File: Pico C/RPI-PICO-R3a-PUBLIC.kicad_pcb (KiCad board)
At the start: 2 copper layers, 53.7 x 21 mm, 54 parts, among them IC1 W25Q16JVUXIQ, J3 USB_C_Receptacle_USB2.0_16P, J4 SM03B-SRSS-TB, Q1 DMG1012T-7, U1 RP2040, U2 RT6150B-33GQW, Y1 ECS-120-8-33-JGN-TR

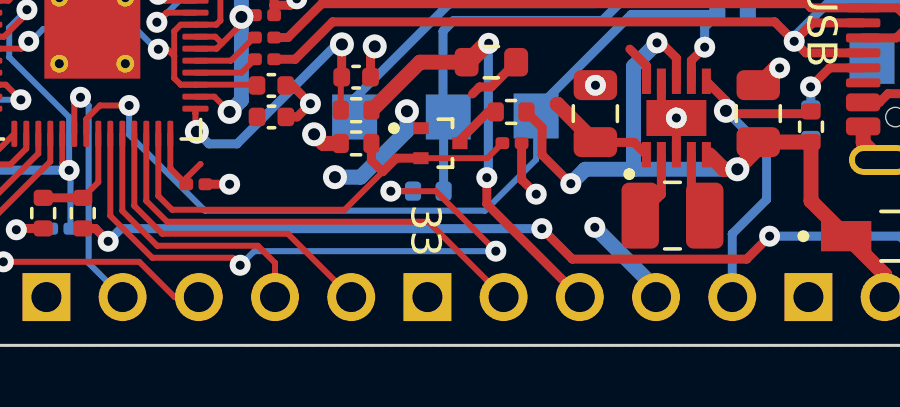
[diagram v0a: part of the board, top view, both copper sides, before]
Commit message: Add files via upload
Corrected pin 33 to actually be GND instead of a NC to GNDA.
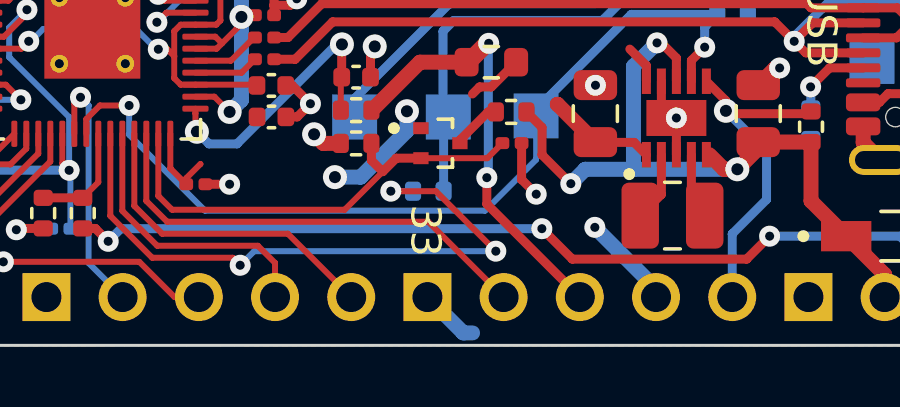
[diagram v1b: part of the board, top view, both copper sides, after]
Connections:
- J2 pad 33: GNDA -> GND
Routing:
- net GND: track 40.8 -> 42.8 mm

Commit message: Add files via upload
Updated component references to more closely match the original Pico.
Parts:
- renumbered R15 to R14, R14 to R15, IC1 to U3, Y1 to X1
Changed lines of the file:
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@@
 	(net 12 "/3V3_EN")
 	(net 13 "Net-(J3-CC1)")
-	(net 14 "unconnected-(IC1-EP-Pad9)")
+	(net 14 "unconnected-(U3-EP-Pad9)")
 	(net 15 "Net-(Q1-D)")
 	(net 16 "+1V1")
@@
 		(descr "Resistor SMD 0201 (0603 Metric), square (rectangular) end terminal, IPC_7351 nominal, (Body size source: https://www.vishay.com/docs/20052/crcw0201e3.pdf), generated with kicad-footprint-generator")
 		(tags "resistor")
-		(property "Reference" "R15"
+		(property "Reference" "R14"
 			(at 0 -1.05 0)
 			(layer "F.Fab")
@@
 		(descr "Resistor SMD 0201 (0603 Metric), square (rectangular) end terminal, IPC_7351 nominal, (Body size source: https://www.vishay.com/docs/20052/crcw0201e3.pdf), generated with kicad-footprint-generator")
 		(tags "resistor")
-		(property "Reference" "R14"
+		(property "Reference" "R15"
 			(at 0 -1.05 0)
 			(layer "F.Fab")
@@
 		(layer "F.Cu")
 		(at 135.625 97.525 -90)
-		(property "Reference" "Y1"
+		(property "Reference" "X1"
 			(at 0.03 -2.1 90)
 			(layer "F.Fab")
@@
 		(at 156.6 97)
 		(descr "<b>USON 2x3x0.6-mm</b><br>")
-		(property "Reference" "IC1"
+		(property "Reference" "U3"
 			(at 0 0 0)
 			(layer "F.Fab")
@@
 			(size 1.65 0.25)
 			(layers "F.Cu" "F.Paste" "F.Mask")
-			(net 14 "unconnected-(IC1-EP-Pad9)")
+			(net 14 "unconnected-(U3-EP-Pad9)")
 			(pinfunction "EP")
 			(pintype "bidirectional+no_connect")

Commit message: Add files via upload
Changed resistor reference numbers to match the real Pico H.
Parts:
- renumbered R3 to R1, R12 to R10, R13 to R11, R14 to R12, R15 to R13, R16 to R14, R17 to R15, R1 to R16, R2 to R17, R4 to R2, R5 to R3, R6 to R4, R7 to R5, R8 to R6, R9 to R7, R10 to R8, R11 to R9
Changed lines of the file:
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@@
 	(net 62 "XOUT")
 	(net 63 "/RP2040/USB_DMX")
-	(net 64 "Net-(R13-Pad2)")
+	(net 64 "Net-(R11-Pad2)")
 	(footprint "Resistor_SMD:R_0402_1005Metric"
 		(layer "F.Cu")
@@
 		(descr "Resistor SMD 0402 (1005 Metric), square (rectangular) end terminal, IPC_7351 nominal, (Body size source: IPC-SM-782 page 72, https://www.pcb-3d.com/wordpress/wp-content/uploads/ipc-sm-782a_amendment_1_and_2.pdf), generated with kicad-footprint-generator")
 		(tags "resistor")
-		(property "Reference" "R6"
+		(property "Reference" "R4"
 			(at 0 -1.17 0)
 			(layer "F.Fab")
@@
 		(descr "Resistor SMD 0402 (1005 Metric), square (rectangular) end terminal, IPC_7351 nominal, (Body size source: IPC-SM-782 page 72, https://www.pcb-3d.com/wordpress/wp-content/uploads/ipc-sm-782a_amendment_1_and_2.pdf), generated with kicad-footprint-generator")
 		(tags "resistor")
-		(property "Reference" "R7"
+		(property "Reference" "R5"
 			(at 0 -1.17 0)
 			(layer "F.Fab")
@@
 		(descr "Resistor SMD 0402 (1005 Metric), square (rectangular) end terminal, IPC_7351 nominal, (Body size source: IPC-SM-782 page 72, https://www.pcb-3d.com/wordpress/wp-content/uploads/ipc-sm-782a_amendment_1_and_2.pdf), generated with kicad-footprint-generator")
 		(tags "resistor")
-		(property "Reference" "R12"
+		(property "Reference" "R10"
 			(at 0 -1.17 90)
 			(layer "F.Fab")
@@
 		(descr "Resistor SMD 0201 (0603 Metric), square (rectangular) end terminal, IPC_7351 nominal, (Body size source: https://www.vishay.com/docs/20052/crcw0201e3.pdf), generated with kicad-footprint-generator")
 		(tags "resistor")
-		(property "Reference" "R14"
+		(property "Reference" "R12"
 			(at 0 -1.05 0)
 			(layer "F.Fab")
@@
 		(descr "Resistor SMD 0402 (1005 Metric), square (rectangular) end terminal, IPC_7351 nominal, (Body size source: IPC-SM-782 page 72, https://www.pcb-3d.com/wordpress/wp-content/uploads/ipc-sm-782a_amendment_1_and_2.pdf), generated with kicad-footprint-generator")
 		(tags "resistor")
-		(property "Reference" "R3"
+		(property "Reference" "R1"
 			(at 0 -1.17 90)
 			(layer "F.Fab")
@@
 		(descr "Resistor SMD 0603 (1608 Metric), square (rectangular) end terminal, IPC_7351 nominal, (Body size source: IPC-SM-782 page 72, https://www.pcb-3d.com/wordpress/wp-content/uploads/ipc-sm-782a_amendment_1_and_2.pdf), generated with kicad-footprint-generator")
 		(tags "resistor")
-		(property "Reference" "R9"
+		(property "Reference" "R7"
 			(at 0 -1.43 0)
 			(layer "F.Fab")
@@
 		(descr "Resistor SMD 0402 (1005 Metric), square (rectangular) end terminal, IPC_7351 nominal, (Body size source: IPC-SM-782 page 72, https://www.pcb-3d.com/wordpress/wp-content/uploads/ipc-sm-782a_amendment_1_and_2.pdf), generated with kicad-footprint-generator")
 		(tags "resistor")
-		(property "Reference" "R17"
+		(property "Reference" "R15"
 			(at 0 -1.17 90)
 			(layer "F.Fab")
@@
 		(descr "Resistor SMD 0402 (1005 Metric), square (rectangular) end terminal, IPC_7351 nominal, (Body size source: IPC-SM-782 page 72, https://www.pcb-3d.com/wordpress/wp-content/uploads/ipc-sm-782a_amendment_1_and_2.pdf), generated with kicad-footprint-generator")
 		(tags "resistor")
-		(property "Reference" "R16"
+		(property "Reference" "R14"
 			(at 0 -1.17 90)
 			(layer "F.Fab")
@@
 		(descr "Resistor SMD 0402 (1005 Metric), square (rectangular) end terminal, IPC_7351 nominal, (Body size source: IPC-SM-782 page 72, https://www.pcb-3d.com/wordpress/wp-content/uploads/ipc-sm-782a_amendment_1_and_2.pdf), generated with kicad-footprint-generator")
 		(tags "resistor")
-		(property "Reference" "R8"
+		(property "Reference" "R6"
 			(at 0 -1.17 0)
 			(layer "F.Fab")
@@
 		(descr "Resistor SMD 0402 (1005 Metric), square (rectangular) end terminal, IPC_7351 nominal, (Body size source: IPC-SM-782 page 72, https://www.pcb-3d.com/wordpress/wp-content/uploads/ipc-sm-782a_amendment_1_and_2.pdf), generated with kicad-footprint-generator")
 		(tags "resistor")
-		(property "Reference" "R4"
+		(property "Reference" "R2"
 			(at 0 -1.27 90)
 			(layer "F.Fab")
@@
 		(descr "Resistor SMD 0201 (0603 Metric), square (rectangular) end terminal, IPC_7351 nominal, (Body size source: https://www.vishay.com/docs/20052/crcw0201e3.pdf), generated with kicad-footprint-generator")
 		(tags "resistor")
-		(property "Reference" "R15"
+		(property "Reference" "R13"
 			(at 0 -1.05 0)
 			(layer "F.Fab")
@@
 			(size 1.05 0.65)
 			(layers "F.Cu" "F.Paste" "F.Mask")
-			(net 64 "Net-(R13-Pad2)")
+			(net 64 "Net-(R11-Pad2)")
 			(pinfunction "1")
 			(pintype "unspecified")
@@
 			(size 1.05 0.65)
 			(layers "F.Cu" "F.Paste" "F.Mask")
-			(net 64 "Net-(R13-Pad2)")
+			(net 64 "Net-(R11-Pad2)")
 			(pinfunction "2")
 			(pintype "unspecified")
@@
 		(descr "Resistor SMD 0402 (1005 Metric), square (rectangular) end terminal, IPC_7351 nominal, (Body size source: IPC-SM-782 page 72, https://www.pcb-3d.com/wordpress/wp-content/uploads/ipc-sm-782a_amendment_1_and_2.pdf), generated with kicad-footprint-generator")
 		(tags "resistor")
-		(property "Reference" "R13"
+		(property "Reference" "R11"
 			(at 0 -1.17 0)
 			(layer "F.Fab")
@@
 			(layers "F.Cu" "F.Paste" "F.Mask")
 			(roundrect_rratio 0.25)
-			(net 64 "Net-(R13-Pad2)")
+			(net 64 "Net-(R11-Pad2)")
 			(pintype "passive")
 		)
@@
 		(descr "Resistor SMD 0402 (1005 Metric), square (rectangular) end terminal, IPC_7351 nominal, (Body size source: IPC-SM-782 page 72, https://www.pcb-3d.com/wordpress/wp-content/uploads/ipc-sm-782a_amendment_1_and_2.pdf), generated with kicad-footprint-generator")
 		(tags "resistor")
-		(property "Reference" "R11"
+		(property "Reference" "R9"
 			(at 0 -1.17 0)
 			(layer "F.Fab")
@@
 		(descr "Resistor SMD 0402 (1005 Metric), square (rectangular) end terminal, IPC_7351 nominal, (Body size source: IPC-SM-782 page 72, https://www.pcb-3d.com/wordpress/wp-content/uploads/ipc-sm-782a_amendment_1_and_2.pdf), generated with kicad-footprint-generator")
 		(tags "resistor")
-		(property "Reference" "R10"
+		(property "Reference" "R8"
 			(at 0.062879 1.301342 0)
 			(layer "B.Fab")
@@
 			(size 1.5 1.5)
 			(layers "B.Cu" "B.Mask")
-			(net 64 "Net-(R13-Pad2)")
+			(net 64 "Net-(R11-Pad2)")
 			(pinfunction "1")
 			(pintype "passive")
@@
 		(descr "Resistor SMD 0402 (1005 Metric), square (rectangular) end terminal, IPC_7351 nominal, (Body size source: IPC-SM-782 page 72, https://www.pcb-3d.com/wordpress/wp-content/uploads/ipc-sm-782a_amendment_1_and_2.pdf), generated with kicad-footprint-generator")
 		(tags "resistor")
-		(property "Reference" "R5"
+		(property "Reference" "R3"
 			(at 0 1.17 0)
 			(layer "B.Fab")
@@
 		(descr "Resistor SMD 0402 (1005 Metric), square (rectangular) end terminal, IPC_7351 nominal, (Body size source: IPC-SM-782 page 72, https://www.pcb-3d.com/wordpress/wp-content/uploads/ipc-sm-782a_amendment_1_and_2.pdf), generated with kicad-footprint-generator")
 		(tags "resistor")
-		(property "Reference" "R2"
+		(property "Reference" "R17"
 			(at 0 -1.25 90)
 			(layer "B.Fab")
@@
 		(descr "Resistor SMD 0402 (1005 Metric), square (rectangular) end terminal, IPC_7351 nominal, (Body size source: IPC-SM-782 page 72, https://www.pcb-3d.com/wordpress/wp-content/uploads/ipc-sm-782a_amendment_1_and_2.pdf), generated with kicad-footprint-generator")
 		(tags "resistor")
-		(property "Reference" "R1"
+		(property "Reference" "R16"
 			(at 0.153641 1.27 90)
 			(layer "B.Fab")

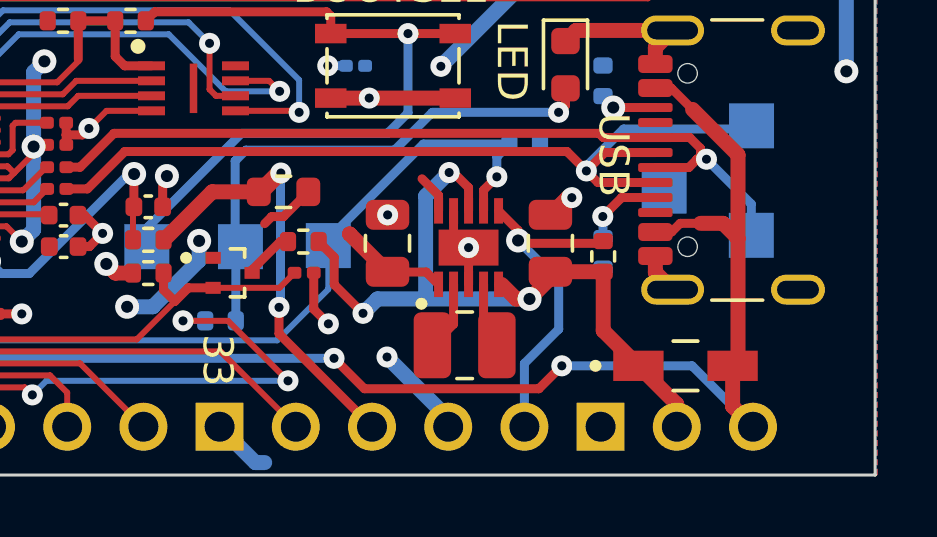
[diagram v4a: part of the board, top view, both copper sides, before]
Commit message: Footprint Modifications
Changed the footprints to use included KiCad models where possible, removed unnecessary STEP files.
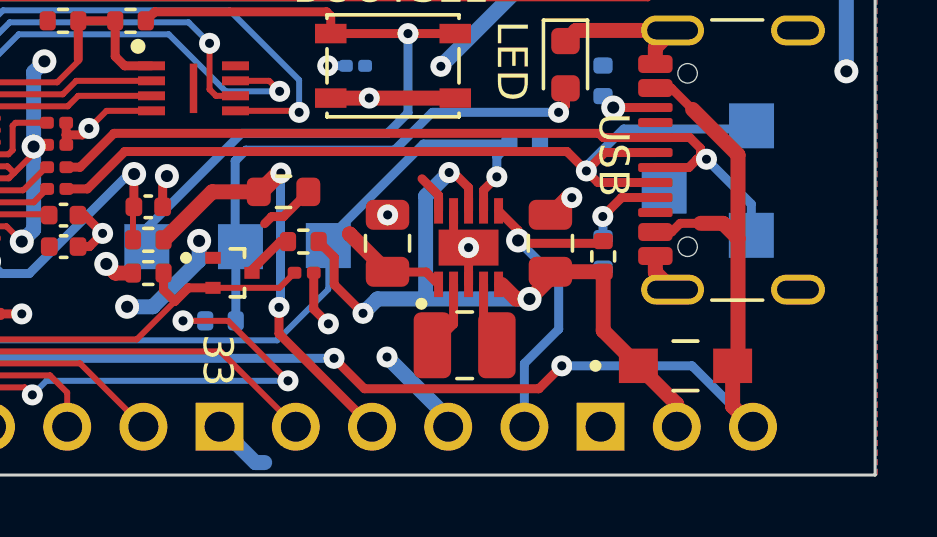
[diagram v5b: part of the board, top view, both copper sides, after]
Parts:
- removed S1: PTS810 SJM 250 SMTR LFS, Pico_C:SW_SPST_PTS810
- added SW1: PTS810 SJM 250 SMTR LFSPTS810 SJM 250 SMTR LFS, Pico_C:SW_SPST_PTS810, F.Cu at (163.2, 96.2)

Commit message: Updated schematic for crystal
Updated the schematic symbol for the 12MHz crystal to be a KiCad included symbol.
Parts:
- removed X1: ECS-120-8-33-JGN-TR, Pico_C:XTAL_ECS-120-8-33-JGN-TR
- added Y1: ECS-120-8-33-JGN-TR, Pico_C:XTAL_ECS-120-8-33-JGN-TR, F.Cu at (135.6, 97.5)
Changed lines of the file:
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@@
 		)
 	)
+	(footprint "Pico_C:XTAL_ECS-120-8-33-JGN-TR"
+		(layer "F.Cu")
+		(at 135.625 97.525 -90)
+		(property "Reference" "Y1"
+			(at 0.03 -2.1 90)
+			(layer "F.Fab")
+			(effects
+				(font
+					(size 0.5 0.5)
+					(thickness 0.1)
+					(bold yes)
+				)
+			)
+		)
+		(property "Value" "ECS-120-8-33-JGN-TR"
+			(at -0.01 2.2 90)
+			(layer "F.Fab")
+			(effects
+				(font
+					(size 0.5 0.5)
+					(thickness 0.1)
+					(bold yes)
+				)
+			)
+		)
+		(property "Footprint" "Pico_C:XTAL_ECS-120-8-33-JGN-TR"
+			(at 0 0 -90)
+			(unlocked yes)
+			(layer "F.Fab")
+			(hide yes)
+			(effects
+				(font
+					(size 1.27 1.27)
+				)
+			)
+		)
+		(property "Datasheet" ""
+			(at 0 0 -90)
+			(unlocked yes)
+			(layer "F.Fab")
+			(hide yes)
+			(effects
+				(font
+					(size 1.27 1.27)
+				)
+			)
+		)
+		(property "Description" "Four pin crystal, GND on pins 2 and 4"
+			(at 0 0 -90)
+			(unlocked yes)
+			(layer "F.Fab")
+			(hide yes)
+			(effects
+				(font
+					(size 1.27 1.27)
+				)
+			)
+		)
+		(property ki_fp_filters "Crystal*")
+		(sheetname "Root")
+		(sheetfile "RPI-PICO-R3a-PUBLIC.kicad_sch")
+		(attr smd)
+		(fp_line
+			(start -0.27 1.25)
+			(end 0.27 1.25)
+			(stroke
+				(width 0.127)
+				(type solid)
+			)
+			(layer "F.SilkS")
+		)
+		(fp_line
+			(start 0.27 -1.25)
+			(end -0.27 -1.25)
+			(stroke
+				(width 0.127)
+				(type solid)
+			)
+			(layer "F.SilkS")
+		)
+		(fp_circle
+			(center -2.11 1.78)
+			(end -2.01 1.78)
+			(stroke
+				(width 0.2)
+				(type solid)
+			)
+			(fill none)
+			(layer "F.SilkS")
+		)
+		(fp_line
+			(start -2.05 1.7)
+			(end 2.05 1.7)
+			(stroke
+				(width 0.05)
+				(type solid)
+			)
+			(layer "F.CrtYd")
+		)
+		(fp_line
+			(start 2.05 1.7)
+			(end 2.05 -1.7)
+			(stroke
+				(width 0.05)
+				(type solid)
+			)
+			(layer "F.CrtYd")
+		)
+		(fp_line
+			(start -2.05 -1.7)
+			(end -2.05 1.7)
+			(stroke
+				(width 0.05)
+				(type solid)
+			)
+			(layer "F.CrtYd")
+		)
+		(fp_line
+			(start 2.05 -1.7)
+			(end -2.05 -1.7)
+			(stroke
+				(width 0.05)
+				(type solid)
+			)
+			(layer "F.CrtYd")
+		)
+		(fp_line
+			(start -1.6 1.25)
+			(end 1.6 1.25)
+			(stroke
+				(width 0.127)
+				(type solid)
+			)
+			(layer "F.Fab")
+		)
+		(fp_line
+			(start 1.6 1.25)
+			(end 1.6 -1.25)
+			(stroke
+				(width 0.127)
+				(type solid)
+			)
+			(layer "F.Fab")
+		)
+		(fp_line
+			(start -1.6 -1.25)
+			(end -1.6 1.25)
+			(stroke
+				(width 0.127)
+				(type solid)
+			)
+			(layer "F.Fab")
+		)
+		(fp_line
+			(start 1.6 -1.25)
+			(end -1.6 -1.25)
+			(stroke
+				(width 0.127)
+				(type solid)
+			)
+			(layer "F.Fab")
+		)
+		(fp_circle
+			(center -2.11 1.78)
+			(end -2.01 1.78)
+			(stroke
+				(width 0.2)
+				(type solid)
+			)
+			(fill none)
+			(layer "F.Fab")
+		)
+		(pad "1" smd rect
+			(at -1.15 0.9 270)
+			(size 1.3 1.1)
+			(layers "F.Cu" "F.Paste" "F.Mask")
+			(net 8 "XIN")
+			(pinfunction "1")
+			(pintype "passive")
+			(solder_mask_margin 0.102)
+		)
+		(pad "2" smd rect
+			(at 1.15 0.9 270)
+			(size 1.3 1.1)
+			(layers "F.Cu" "F.Paste" "F.Mask")
+			(net 57 "GND")
+			(pinfunction "2")
+			(pintype "passive")
+			(solder_mask_margin 0.102)
+		)
+		(pad "3" smd rect
+			(at 1.15 -0.9 270)
+			(size 1.3 1.1)
+			(layers "F.Cu" "F.Paste" "F.Mask")
+			(net 19 "/XR")
+			(pinfunction "3")
+			(pintype "passive")
+			(solder_mask_margin 0.102)
+		)
+		(pad "4" smd rect
+			(at -1.15 -0.9 270)
+			(size 1.3 1.1)
+			(layers "F.Cu" "F.Paste" "F.Mask")
+			(net 57 "GND")
+			(pinfunction "4")
+			(pintype "passive")
+			(solder_mask_margin 0.102)
+		)
+		(model "${KICAD8_3DMODEL_DIR}/Crystal.3dshapes/Crystal_SMD_3225-4Pin_3.2x2.5mm.step"
+			(offset
+				(xyz 0 0 0)
+			)
+			(scale
+				(xyz 1 1 1)
+			)
+			(rotate
+				(xyz 0 0 0)
+			)
+		)
+	)
 	(footprint "Resistor_SMD:R_0402_1005Metric"
 		(layer "F.Cu")
@@
 			(offset
 				(xyz 0 0 0)
-			)
-			(scale
-				(xyz 1 1 1)
-			)
-			(rotate
-				(xyz 0 0 0)
-			)
-		)
-	)
-	(footprint "Pico_C:XTAL_ECS-120-8-33-JGN-TR"
-		(layer "F.Cu")
-		(at 135.625 97.525 -90)
-		(property "Reference" "X1"
-			(at 0.03 -2.1 90)
-			(layer "F.Fab")
-			(effects
-				(font
-					(size 0.5 0.5)
-					(thickness 0.1)
-					(bold yes)
-				)
-			)
-		)
-		(property "Value" "ECS-120-8-33-JGN-TR"
-			(at -0.01 2.2 90)
-			(layer "F.Fab")
-			(effects
-				(font
-					(size 0.5 0.5)
-					(thickness 0.1)
-					(bold yes)
-				)
-			)
-		)
-		(property "Footprint" "Pico_C:XTAL_ECS-120-8-33-JGN-TR"
-			(at 0 0 -90)
-			(unlocked yes)
-			(layer "F.Fab")
-			(hide yes)
-			(effects
-				(font
-					(size 1.27 1.27)
-				)
-			)
-		)
-		(property "Datasheet" "https://ecsxtal.com/store/pdf/ecx-32.pdf"
-			(at 0 0 -90)
-			(unlocked yes)
-			(layer "F.Fab")
-			(hide yes)
-			(effects
-				(font
-					(size 1.27 1.27)
-				)
-			)
-		)
-		(property "Description" ""
-			(at 0 0 -90)
-			(unlocked yes)
-			(layer "F.Fab")
-			(hide yes)
-			(effects
-				(font
-					(size 1.27 1.27)
-				)
-			)
-		)
-		(sheetname "Root")
-		(sheetfile "RPI-PICO-R3a-PUBLIC.kicad_sch")
-		(attr smd)
-		(fp_line
-			(start -0.27 1.25)
-			(end 0.27 1.25)
-			(stroke
-				(width 0.127)
-				(type solid)
-			)
-			(layer "F.SilkS")
-		)
-		(fp_line
-			(start 0.27 -1.25)
-			(end -0.27 -1.25)
-			(stroke
-				(width 0.127)
-				(type solid)
-			)
-			(layer "F.SilkS")
-		)
-		(fp_circle
-			(center -2.11 1.78)
-			(end -2.01 1.78)
-			(stroke
-				(width 0.2)
-				(type solid)
-			)
-			(fill none)
-			(layer "F.SilkS")
-		)
-		(fp_line
-			(start -2.05 1.7)
-			(end 2.05 1.7)
-			(stroke
-				(width 0.05)
-				(type solid)
-			)
-			(layer "F.CrtYd")
-		)
-		(fp_line
-			(start 2.05 1.7)
-			(end 2.05 -1.7)
-			(stroke
-				(width 0.05)
-				(type solid)
-			)
-			(layer "F.CrtYd")
-		)
-		(fp_line
-			(start -2.05 -1.7)
-			(end -2.05 1.7)
-			(stroke
-				(width 0.05)
-				(type solid)
-			)
-			(layer "F.CrtYd")
-		)
-		(fp_line
-			(start 2.05 -1.7)
-			(end -2.05 -1.7)
-			(stroke
-				(width 0.05)
-				(type solid)
-			)
-			(layer "F.CrtYd")
-		)
-		(fp_line
-			(start -1.6 1.25)
-			(end 1.6 1.25)
-			(stroke
-				(width 0.127)
-				(type solid)
-			)
-			(layer "F.Fab")
-		)
-		(fp_line
-			(start 1.6 1.25)
-			(end 1.6 -1.25)
-			(stroke
-				(width 0.127)
-				(type solid)
-			)
-			(layer "F.Fab")
-		)
-		(fp_line
-			(start -1.6 -1.25)
-			(end -1.6 1.25)
-			(stroke
-				(width 0.127)
-				(type solid)
-			)
-			(layer "F.Fab")
-		)
-		(fp_line
-			(start 1.6 -1.25)
-			(end -1.6 -1.25)
-			(stroke
-				(width 0.127)
-				(type solid)
-			)
-			(layer "F.Fab")
-		)
-		(fp_circle
-			(center -2.11 1.78)
-			(end -2.01 1.78)
-			(stroke
-				(width 0.2)
-				(type solid)
-			)
-			(fill none)
-			(layer "F.Fab")
-		)
-		(pad "1" smd rect
-			(at -1.15 0.9 270)
-			(size 1.3 1.1)
-			(layers "F.Cu" "F.Paste" "F.Mask")
-			(net 8 "XIN")
-			(pinfunction "IN/OUT")
-			(pintype "bidirectional")
-			(solder_mask_margin 0.102)
-		)
-		(pad "2" smd rect
-			(at 1.15 0.9 270)
-			(size 1.3 1.1)
-			(layers "F.Cu" "F.Paste" "F.Mask")
-			(net 57 "GND")
-			(pinfunction "GND")
-			(pintype "power_in")
-			(solder_mask_margin 0.102)
-		)
-		(pad "3" smd rect
-			(at 1.15 -0.9 270)
-			(size 1.3 1.1)
-			(layers "F.Cu" "F.Paste" "F.Mask")
-			(net 19 "/XR")
-			(pinfunction "OUT/IN")
-			(pintype "bidirectional")
-			(solder_mask_margin 0.102)
-		)
-		(pad "4" smd rect
-			(at -1.15 -0.9 270)
-			(size 1.3 1.1)
-			(layers "F.Cu" "F.Paste" "F.Mask")
-			(net 57 "GND")
-			(pinfunction "GND__1")
-			(pintype "power_in")
-			(solder_mask_margin 0.102)
-		)
-		(model "${KICAD8_3DMODEL_DIR}/Crystal.3dshapes/Crystal_SMD_3225-4Pin_3.2x2.5mm.step"
-			(offset
-				(xyz 0 0 0)
